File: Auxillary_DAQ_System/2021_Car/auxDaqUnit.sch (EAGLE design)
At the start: 39 parts, among them IC1 ADS1119IPWT, IC2 TPS563231DRLR, J1 1990083, J10 1990083, J11 1990083, J12 1990083, J2 1990083, J3 1990083, J4 1990083, J5 1990083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

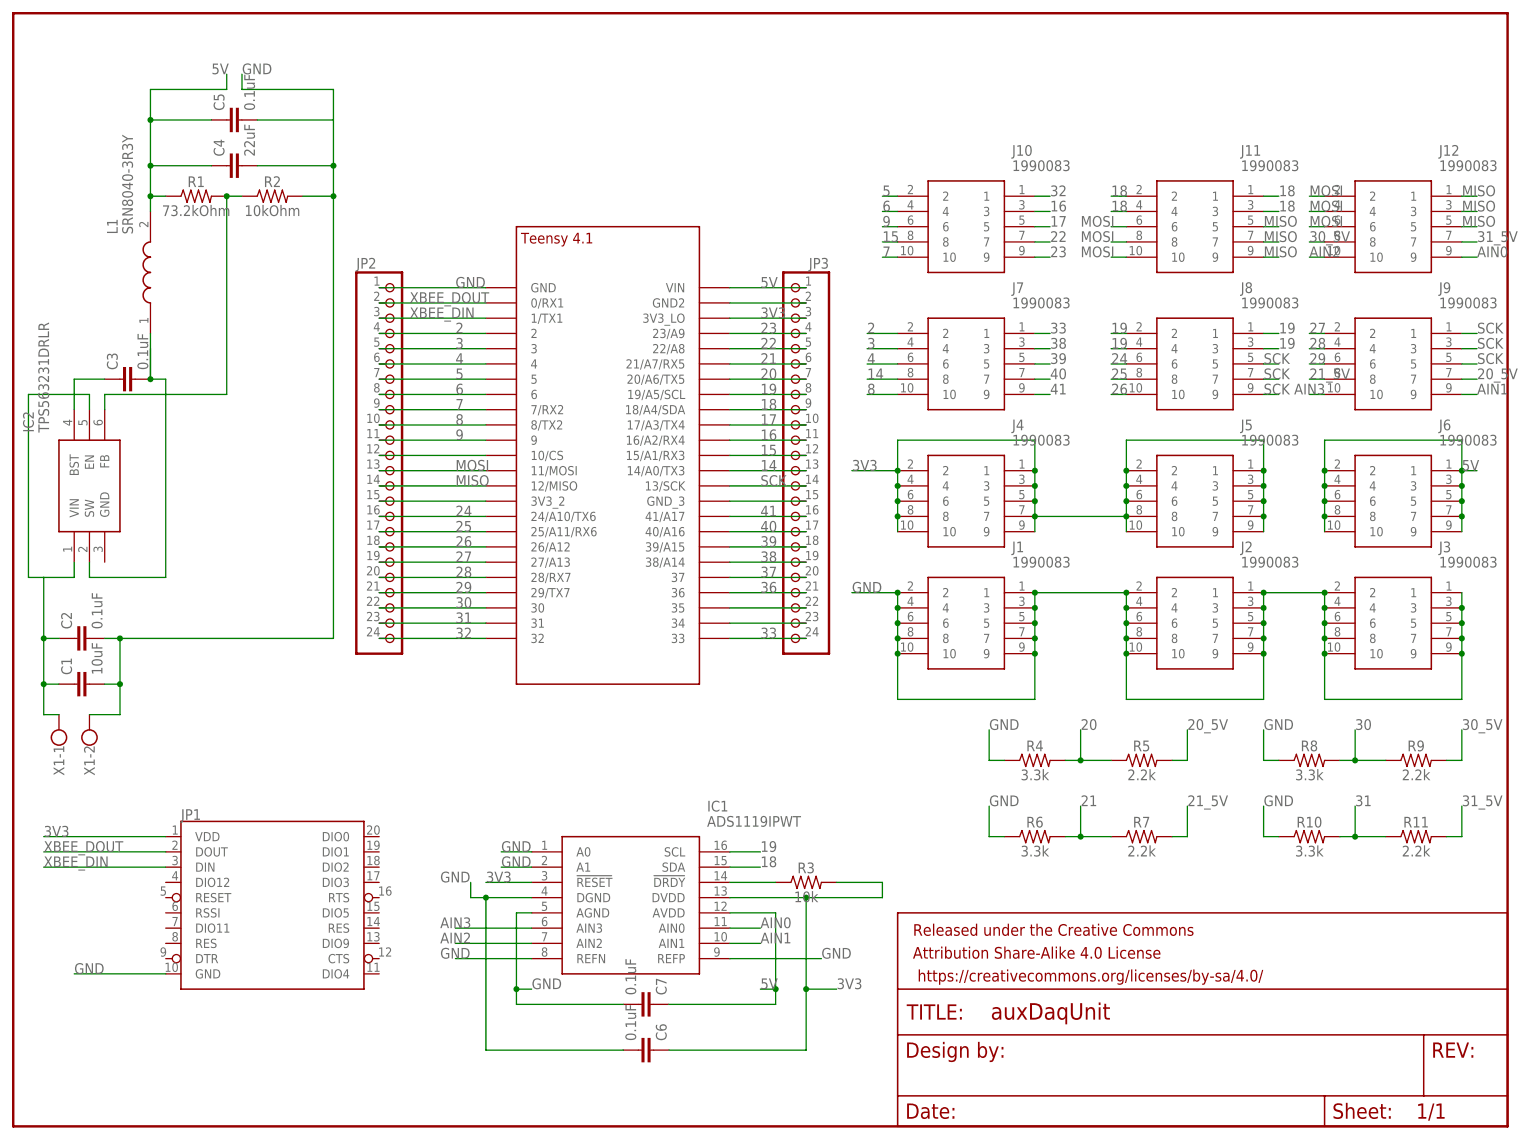
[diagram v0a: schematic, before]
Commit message: updated schematic and pinout
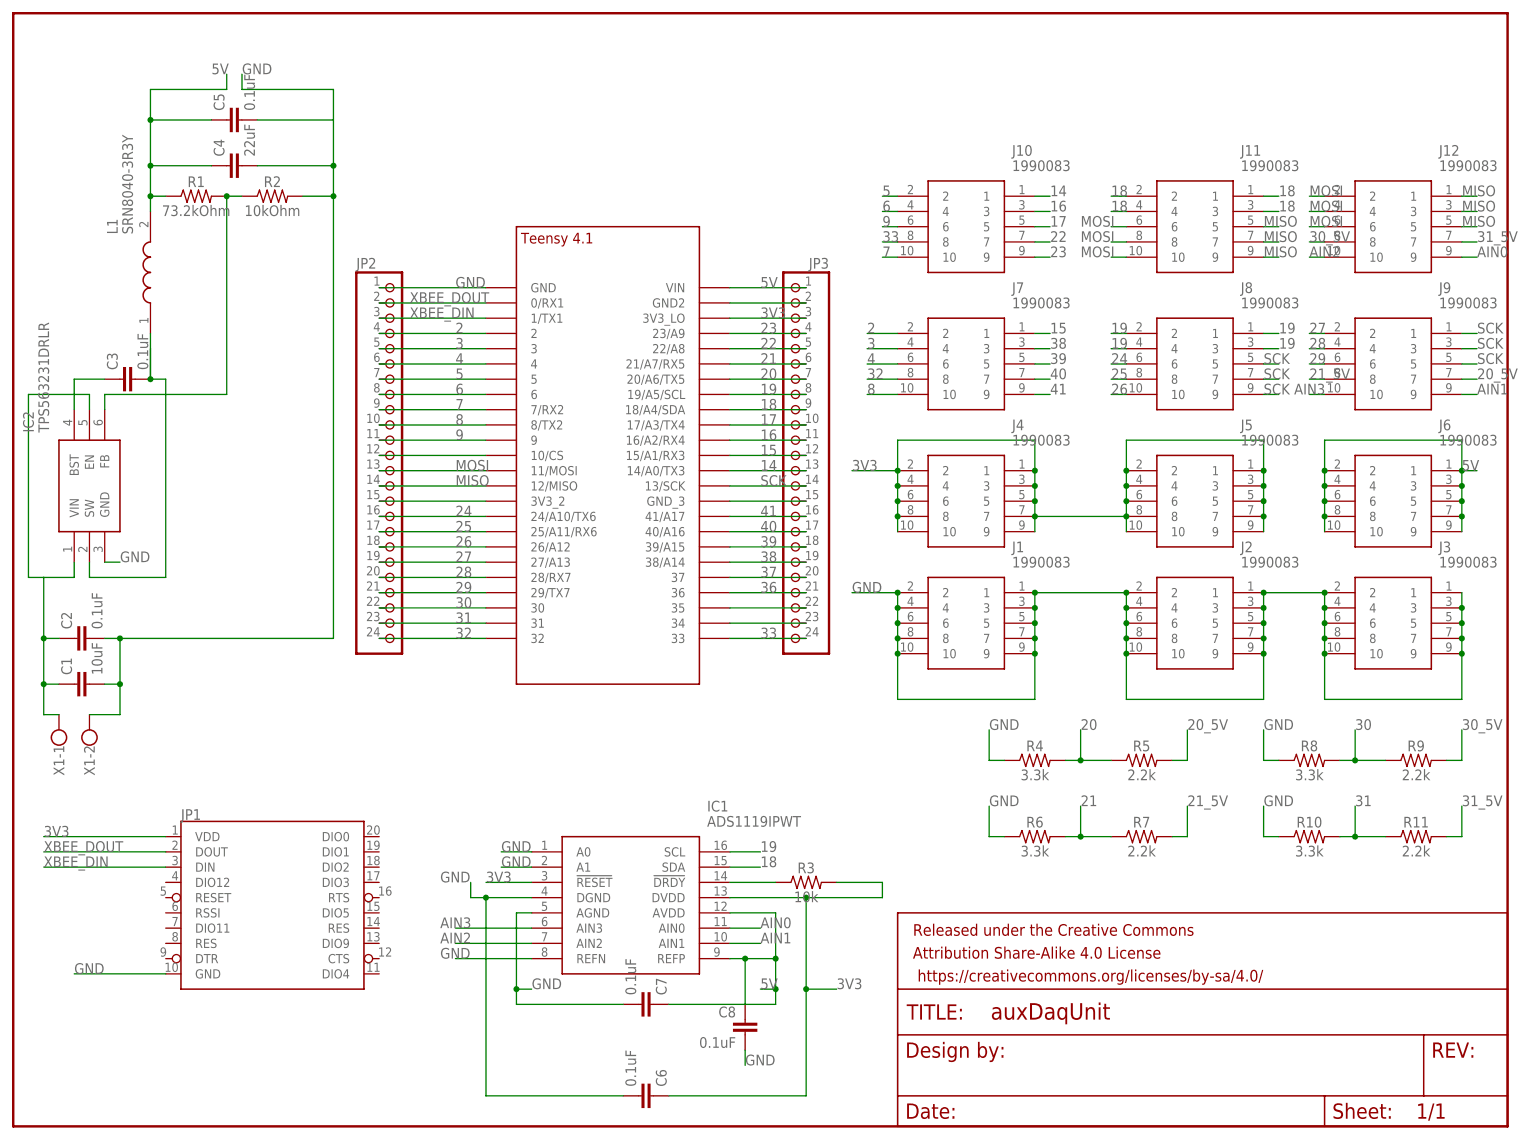
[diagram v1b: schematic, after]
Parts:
- added C8: 0.1uF, SparkFun-Capacitors:0.1UF-0603-25V-(+80/-20%)
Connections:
- net 14: now also J10.1; no longer J7.8
- net 15: now also J7.1; no longer J10.8
- net 32: now also J7.8; no longer J10.1
- net 33: now also J10.8; no longer J7.1
- net 5V: now also C8.1, IC1.REFP
- net GND: now also C8.2, IC2.GND; no longer IC1.REFP
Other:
- moved on the sheet: C6
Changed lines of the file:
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@@
 <?xml version="1.0" encoding="utf-8"?>
 <!DOCTYPE eagle SYSTEM "eagle.dtd">
-<eagle version="9.6.1">
+<eagle version="9.6.2">
 <drawing>
 <settings>
@@
 <part name="R10" library="SparkFun-Resistors" library_urn="urn:adsk.eagle:library:532" deviceset="3.3KOHM" device="-0603-1/10W-1%" package3d_urn="urn:adsk.eagle:package:39650/1" value="3.3k"/>
 <part name="R11" library="SparkFun-Resistors" library_urn="urn:adsk.eagle:library:532" deviceset="2.2KOHM" device="-0603-1/10W-1%" package3d_urn="urn:adsk.eagle:package:39650/1" value="2.2k"/>
+<part name="C8" library="SparkFun-Capacitors" library_urn="urn:adsk.eagle:library:510" deviceset="0.1UF" device="-0603-25V-(+80/-20%)" package3d_urn="urn:adsk.eagle:package:37414/1" value="0.1uF"/>
 </parts>
 <sheets>
@@
 <attribute name="NAME" x="11.811" y="63.5" size="1.778" layer="95" rot="R270"/>
 </instance>
-<instance part="C6" gate="G$1" x="104.14" y="12.7" smashed="yes" rot="MR90">
-<attribute name="NAME" x="107.061" y="14.224" size="1.778" layer="95" font="vector" rot="MR90"/>
-<attribute name="VALUE" x="101.981" y="14.224" size="1.778" layer="96" font="vector" rot="MR90"/>
+<instance part="C6" gate="G$1" x="104.14" y="5.08" smashed="yes" rot="MR90">
+<attribute name="NAME" x="107.061" y="6.604" size="1.778" layer="95" font="vector" rot="MR90"/>
+<attribute name="VALUE" x="101.981" y="6.604" size="1.778" layer="96" font="vector" rot="MR90"/>
 </instance>
 <instance part="C7" gate="G$1" x="104.14" y="20.32" smashed="yes" rot="MR90">
@@
 <attribute name="NAME" x="233.68" y="49.784" size="1.778" layer="95" font="vector" align="bottom-center"/>
 <attribute name="VALUE" x="233.68" y="46.736" size="1.778" layer="96" font="vector" align="top-center"/>
+</instance>
+<instance part="C8" gate="G$1" x="121.92" y="15.24" smashed="yes" rot="MR0">
+<attribute name="NAME" x="120.396" y="18.161" size="1.778" layer="95" font="vector" rot="MR0"/>
+<attribute name="VALUE" x="120.396" y="13.081" size="1.778" layer="96" font="vector" rot="MR0"/>
 </instance>
 </instances>
@@
 <wire x1="119.38" y1="38.1" x2="132.08" y2="38.1" width="0.1524" layer="91"/>
 <wire x1="132.08" y1="38.1" x2="132.08" y2="22.86" width="0.1524" layer="91"/>
-<wire x1="132.08" y1="22.86" x2="132.08" y2="12.7" width="0.1524" layer="91"/>
-<wire x1="132.08" y1="12.7" x2="109.22" y2="12.7" width="0.1524" layer="91"/>
+<wire x1="132.08" y1="22.86" x2="132.08" y2="5.08" width="0.1524" layer="91"/>
+<wire x1="132.08" y1="5.08" x2="109.22" y2="5.08" width="0.1524" layer="91"/>
 <pinref part="C6" gate="G$1" pin="1"/>
 <wire x1="132.08" y1="22.86" x2="137.16" y2="22.86" width="0.1524" layer="91"/>
@@
 <wire x1="76.2" y1="38.1" x2="76.2" y2="40.64" width="0.1524" layer="91"/>
 <pinref part="C6" gate="G$1" pin="2"/>
-<wire x1="101.6" y1="12.7" x2="78.74" y2="12.7" width="0.1524" layer="91"/>
-<wire x1="78.74" y1="12.7" x2="78.74" y2="38.1" width="0.1524" layer="91"/>
+<wire x1="101.6" y1="5.08" x2="78.74" y2="5.08" width="0.1524" layer="91"/>
+<wire x1="78.74" y1="5.08" x2="78.74" y2="38.1" width="0.1524" layer="91"/>
 <junction x="78.74" y="38.1"/>
 <label x="71.12" y="40.64" size="1.778" layer="95"/>
@@
 <wire x1="86.36" y1="27.94" x2="73.66" y2="27.94" width="0.1524" layer="91"/>
 <label x="71.12" y="27.94" size="1.778" layer="95"/>
-</segment>
-<segment>
-<pinref part="IC1" gate="G$1" pin="REFP"/>
-<wire x1="119.38" y1="27.94" x2="134.62" y2="27.94" width="0.1524" layer="91"/>
-<label x="134.62" y="27.94" size="1.778" layer="95"/>
 </segment>
 <segment>
@@
 <label x="208.28" y="53.34" size="1.778" layer="95"/>
 </segment>
+<segment>
+<pinref part="IC2" gate="G$1" pin="GND"/>
+<wire x1="15.24" y1="93.98" x2="17.78" y2="93.98" width="0.1524" layer="91"/>
+<label x="17.78" y="93.98" size="1.778" layer="95"/>
+</segment>
+<segment>
+<pinref part="C8" gate="G$1" pin="2"/>
+<wire x1="121.92" y1="12.7" x2="121.92" y2="10.16" width="0.1524" layer="91"/>
+<label x="121.92" y="10.16" size="1.778" layer="95"/>
+</segment>
 </net>
 <net name="GNDBLOCK" class="0">
@@
 </segment>
 <segment>
-<pinref part="J7" gate="G$1" pin="8"/>
-<wire x1="147.32" y1="124.46" x2="142.24" y2="124.46" width="0.1524" layer="91"/>
-<label x="142.24" y="124.46" size="1.778" layer="95"/>
+<pinref part="J10" gate="G$1" pin="1"/>
+<wire x1="170.18" y1="154.94" x2="172.72" y2="154.94" width="0.1524" layer="91"/>
+<label x="172.72" y="154.94" size="1.778" layer="95"/>
 </segment>
 </net>
@@
 </segment>
 <segment>
-<pinref part="J10" gate="G$1" pin="8"/>
-<wire x1="147.32" y1="147.32" x2="144.78" y2="147.32" width="0.1524" layer="91"/>
-<label x="144.78" y="147.32" size="1.778" layer="95"/>
+<pinref part="J7" gate="G$1" pin="1"/>
+<wire x1="170.18" y1="132.08" x2="172.72" y2="132.08" width="0.1524" layer="91"/>
+<label x="172.72" y="132.08" size="1.778" layer="95"/>
 </segment>
 </net>
@@
 <wire x1="127" y1="20.32" x2="127" y2="22.86" width="0.1524" layer="91"/>
 <pinref part="IC1" gate="G$1" pin="AVDD"/>
-<wire x1="127" y1="22.86" x2="127" y2="35.56" width="0.1524" layer="91"/>
+<wire x1="127" y1="22.86" x2="127" y2="27.94" width="0.1524" layer="91"/>
+<wire x1="127" y1="27.94" x2="127" y2="35.56" width="0.1524" layer="91"/>
 <wire x1="119.38" y1="35.56" x2="127" y2="35.56" width="0.1524" layer="91"/>
 <wire x1="127" y1="22.86" x2="124.46" y2="22.86" width="0.1524" layer="91"/>
 <junction x="127" y="22.86"/>
 <label x="124.46" y="22.86" size="1.778" layer="95"/>
+<pinref part="IC1" gate="G$1" pin="REFP"/>
+<wire x1="119.38" y1="27.94" x2="121.92" y2="27.94" width="0.1524" layer="91"/>
+<junction x="127" y="27.94"/>
+<wire x1="121.92" y1="27.94" x2="127" y2="27.94" width="0.1524" layer="91"/>
+<wire x1="121.92" y1="27.94" x2="121.92" y2="20.32" width="0.1524" layer="91"/>
+<junction x="121.92" y="27.94"/>
+<pinref part="C8" gate="G$1" pin="1"/>
 </segment>
 <segment>
@@
 <net name="32" class="0">
 <segment>
-<pinref part="J10" gate="G$1" pin="1"/>
-<wire x1="170.18" y1="154.94" x2="172.72" y2="154.94" width="0.1524" layer="91"/>
-<label x="172.72" y="154.94" size="1.778" layer="95"/>
-</segment>
-<segment>
 <pinref part="JP2" gate="A" pin="24"/>
 <pinref part="U$1" gate="G$1" pin="32"/>
@@
 <label x="73.66" y="81.28" size="1.778" layer="95"/>
 </segment>
+<segment>
+<pinref part="J7" gate="G$1" pin="8"/>
+<wire x1="147.32" y1="124.46" x2="142.24" y2="124.46" width="0.1524" layer="91"/>
+<label x="142.24" y="124.46" size="1.778" layer="95"/>
+</segment>
 </net>
 <net name="33" class="0">
-<segment>
-<pinref part="J7" gate="G$1" pin="1"/>
-<wire x1="170.18" y1="132.08" x2="172.72" y2="132.08" width="0.1524" layer="91"/>
-<label x="172.72" y="132.08" size="1.778" layer="95"/>
-</segment>
 <segment>
 <pinref part="U$1" gate="G$1" pin="33"/>
@@
 <label x="124.46" y="81.28" size="1.778" layer="95"/>
 </segment>
-</net>
+<segment>
+<pinref part="J10" gate="G$1" pin="8"/>
+<wire x1="147.32" y1="147.32" x2="144.78" y2="147.32" width="0.1524" layer="91"/>
+<label x="144.78" y="147.32" size="1.778" layer="95"/>
+</segment>
+</net>

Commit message: Fixed minor airwires
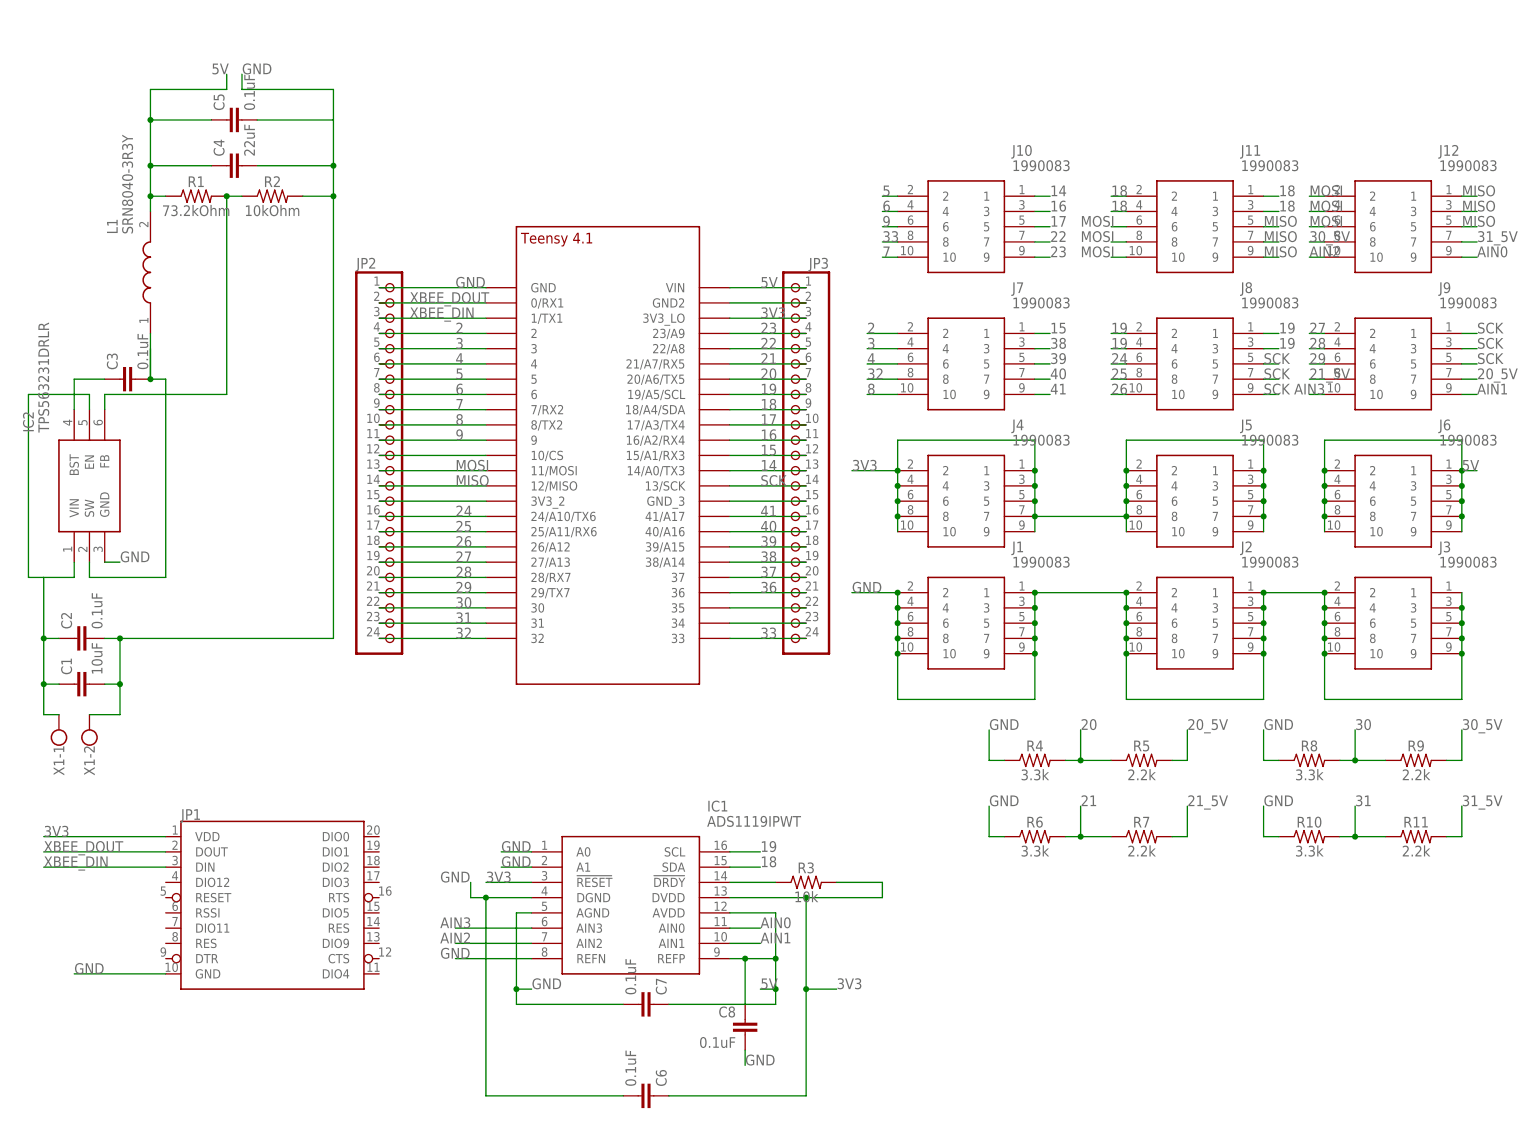
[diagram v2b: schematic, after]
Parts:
- removed FRAME1: FRAME-LETTER, SparkFun-Aesthetics:FRAME-LETTER
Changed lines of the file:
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@@
 <?xml version="1.0" encoding="utf-8"?>
 <!DOCTYPE eagle SYSTEM "eagle.dtd">
-<eagle version="9.6.2">
+<eagle version="9.6.1">
 <drawing>
 <settings>
@@
 </classes>
 <parts>
-<part name="FRAME1" library="SparkFun-Aesthetics" library_urn="urn:adsk.eagle:library:507" deviceset="FRAME-LETTER" device="" package3d_urn="urn:adsk.eagle:package:37121/1"/>
 <part name="JP1" library="SparkFun-RF" library_urn="urn:adsk.eagle:library:531" deviceset="XBEE" device="" package3d_urn="urn:adsk.eagle:package:39572/1"/>
 <part name="J1" library="1990083" deviceset="1990083" device=""/>
@@
 </plain>
 <instances>
-<instance part="FRAME1" gate="G$1" x="0" y="0" smashed="yes"/>
-<instance part="FRAME1" gate="V" x="147.32" y="0" smashed="yes">
-<attribute name="LAST_DATE_TIME" x="160.02" y="1.27" size="2.54" layer="94" font="vector"/>
-<attribute name="SHEET" x="233.68" y="1.27" size="2.54" layer="94" font="vector"/>
-<attribute name="DRAWING_NAME" x="162.814" y="17.78" size="2.7432" layer="94" font="vector"/>
-</instance>
 <instance part="JP1" gate="G$1" x="43.18" y="38.1" smashed="yes">
 <attribute name="NAME" x="27.94" y="51.054" size="1.778" layer="95" font="vector"/>
